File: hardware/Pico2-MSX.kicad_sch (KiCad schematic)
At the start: 63 parts, among them J1 DEBUG, J2 USB_C, SW1 BOOT, U1 MCP4922-ESL, U2 TXB0108PW, U3 W25Q128JVS, U4 W25Q128JVS, U6 RP2350_80QFN, U7 MC74LCX32DTR2G, U8 AMS1117-3.3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

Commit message: Improving the 1v1 circuit
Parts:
- C16, C17: footprint Capacitor_SMD:C_0603_1608Metric -> Additional:C_0603_1608Metric_small
- L1: footprint Inductor_SMD:L_1008_2520Metric -> Additional:L_pol_2016
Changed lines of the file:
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@@
 			)
 		)
-		(property "Footprint" "Inductor_SMD:L_1008_2520Metric"
+		(property "Footprint" "Additional:L_pol_2016"
 			(at 144.78 107.95 0)
 			(effects
@@
 			)
 		)
-		(property "Footprint" "Capacitor_SMD:C_0603_1608Metric"
+		(property "Footprint" "Additional:C_0603_1608Metric_small"
 			(at 133.0452 111.76 0)
 			(effects
@@
 			)
 		)
-		(property "Footprint" "Capacitor_SMD:C_0603_1608Metric"
+		(property "Footprint" "Additional:C_0603_1608Metric_small"
 			(at 120.3452 111.76 0)
 			(effects

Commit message: Delete via for flash memory
And other small modifications (reference at JLCPCB)
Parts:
- J1: LCSC (none) -> C24980
- J2: LCSC C5362630 -> C2988369
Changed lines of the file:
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@@
 			)
 		)
-		(property "LCSC" "C5362630"
+		(property "LCSC" "C2988369"
 			(at 40.64 50.8 0)
 			(effects
@@
 			(at 138.43 179.07 0)
 			(effects
+				(font
+					(size 1.27 1.27)
+				)
+				(hide yes)
+			)
+		)
+		(property "LCSC" "C24980"
+			(at 138.43 179.07 0)
+			(effects

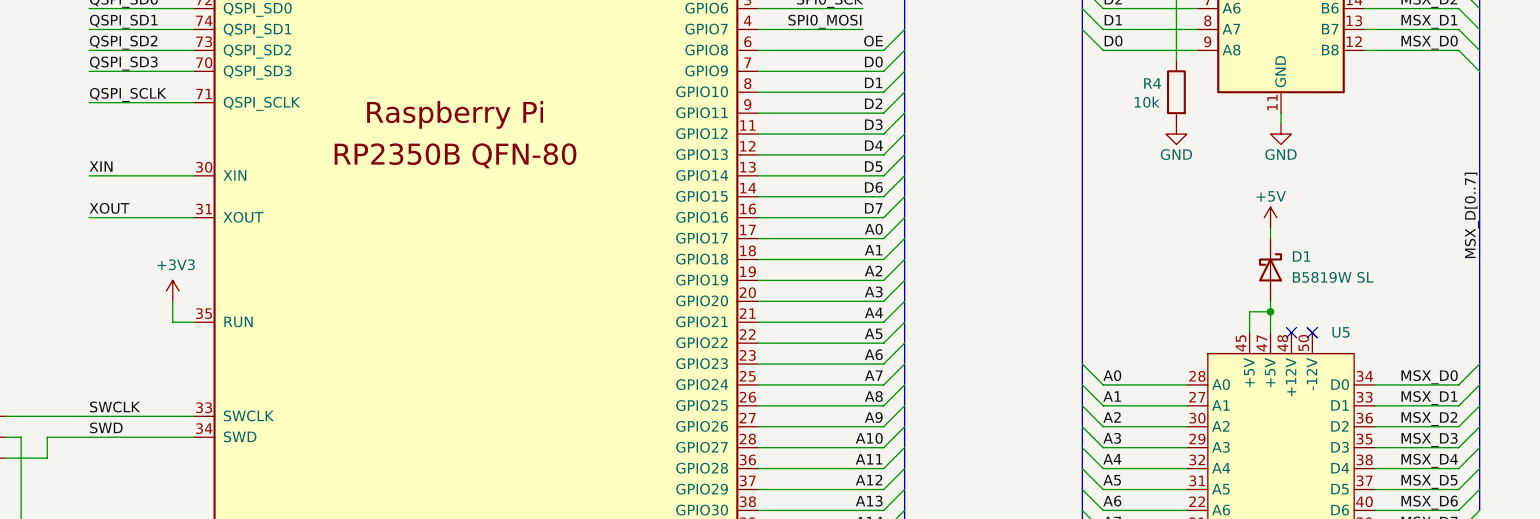
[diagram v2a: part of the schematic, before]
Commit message: Cost reduction and correction of fixing hole placement
- The via are now at a minimum hole size of 0.25.
- The 0201 capacitors have been replaced by 0402s.
- The fixing holes have been moved to a position closer to the standard.
- The tracks have been widened outside the RP2350 area.
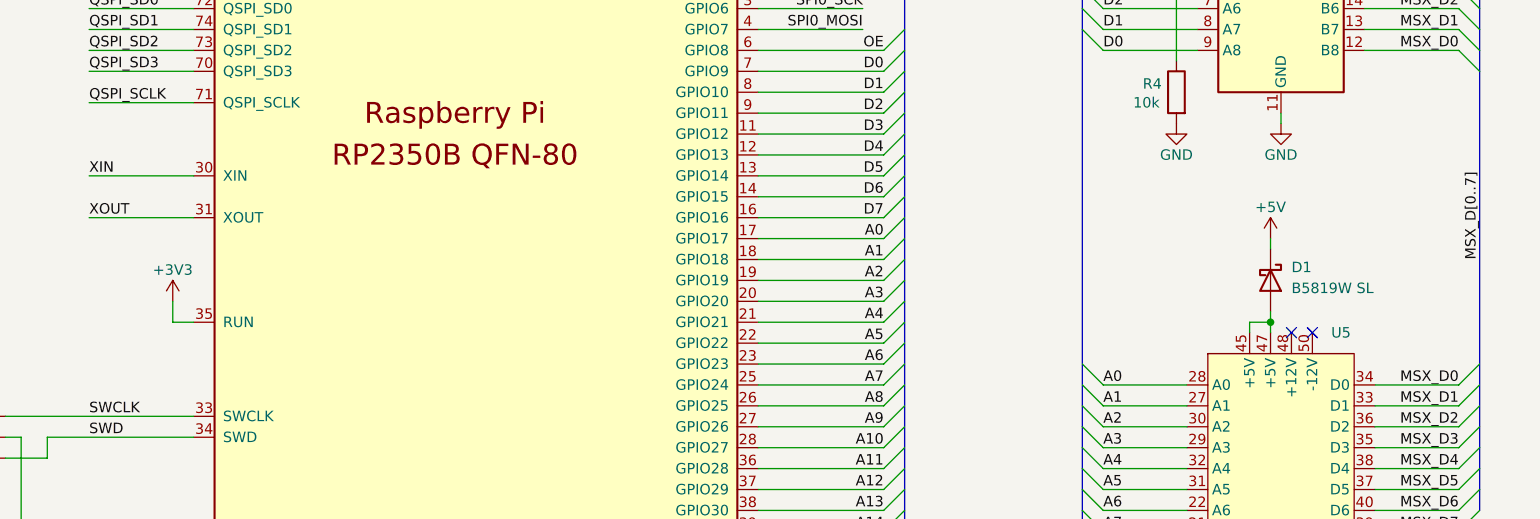
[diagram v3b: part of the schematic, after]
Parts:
- C10, C11, C12, C13, C14, C19, C20, C21, C22, C5, C6, C7: footprint Capacitor_SMD:C_0201_0603Metric -> Additional:C_0402_1005Metric_thin; LCSC C307380 -> C307331
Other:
- moved on the sheet: D1
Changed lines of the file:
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@@
 	)
 	(junction
+		(at 297.18 165.1)
+		(diameter 0)
+		(color 0 0 0 0)
+	)
+	(junction
 		(at 279.4 71.12)
 		(diameter 0)
@@
 	)
 	(junction
-		(at 297.18 163.83)
-		(diameter 0)
-		(color 0 0 0 0)
-	)
-	(junction
 		(at 144.78 35.56)
 		(diameter 0)
@@
 	(wire
 		(pts
+			(xy 297.18 165.1) (xy 297.18 166.37)
+		)
+		(stroke
+			(width 0)
+			(type default)
+		)
+	)
+	(wire
+		(pts
 			(xy 199.39 81.28) (xy 201.93 81.28)
 		)
@@
 	(wire
 		(pts
-			(xy 294.64 163.83) (xy 297.18 163.83)
+			(xy 294.64 165.1) (xy 297.18 165.1)
 		)
 		(stroke
@@
 	(wire
 		(pts
-			(xy 294.64 166.37) (xy 294.64 163.83)
+			(xy 294.64 166.37) (xy 294.64 165.1)
 		)
 		(stroke
@@
 	(wire
 		(pts
-			(xy 297.18 162.56) (xy 297.18 163.83)
-		)
-		(stroke
-			(width 0)
-			(type default)
-		)
-	)
-	(wire
-		(pts
 			(xy 80.01 130.81) (xy 92.71 130.81)
 		)
@@
 	(wire
 		(pts
-			(xy 297.18 153.67) (xy 297.18 154.94)
+			(xy 297.18 154.94) (xy 297.18 156.21)
 		)
 		(stroke
@@
 	(wire
 		(pts
-			(xy 297.18 163.83) (xy 297.18 166.37)
+			(xy 297.18 163.83) (xy 297.18 165.1)
 		)
 		(stroke
@@
 			)
 		)
-		(property "Footprint" "Capacitor_SMD:C_0201_0603Metric"
+		(property "Footprint" "Additional:C_0402_1005Metric_thin"
 			(at 254.9652 69.85 0)
 			(effects
@@
 			)
 		)
-		(property "LCSC" "C307380"
+		(property "LCSC" "C307331"
 			(at 254 66.04 0)
 			(effects
@@
 			)
 		)
-		(property "Footprint" "Capacitor_SMD:C_0201_0603Metric"
+		(property "Footprint" "Additional:C_0402_1005Metric_thin"
 			(at 267.6652 69.85 0)
 			(effects
@@
 			)
 		)
-		(property "LCSC" "C307380"
+		(property "LCSC" "C307331"
 			(at 266.7 66.04 0)
 			(effects
@@
 			)
 		)
-		(property "Footprint" "Capacitor_SMD:C_0201_0603Metric"
+		(property "Footprint" "Additional:C_0402_1005Metric_thin"
 			(at 280.3652 69.85 0)
 			(effects
@@
 			)
 		)
-		(property "LCSC" "C307380"
+		(property "LCSC" "C307331"
 			(at 279.4 66.04 0)
 			(effects
@@
 			)
 		)
-		(property "Footprint" "Capacitor_SMD:C_0201_0603Metric"
+		(property "Footprint" "Additional:C_0402_1005Metric_thin"
 			(at 293.0652 69.85 0)
 			(effects
@@
 			)
 		)
-		(property "LCSC" "C307380"
+		(property "LCSC" "C307331"
 			(at 292.1 66.04 0)
 			(effects
@@
 			)
 		)
-		(property "Footprint" "Capacitor_SMD:C_0201_0603Metric"
+		(property "Footprint" "Additional:C_0402_1005Metric_thin"
 			(at 305.7652 69.85 0)
 			(effects
@@
 			)
 		)
-		(property "LCSC" "C307380"
+		(property "LCSC" "C307331"
 			(at 304.8 66.04 0)
 			(effects
@@
 			)
 		)
-		(property "Footprint" "Capacitor_SMD:C_0201_0603Metric"
+		(property "Footprint" "Additional:C_0402_1005Metric_thin"
 			(at 318.4652 69.85 0)
 			(effects
@@
 			)
 		)
-		(property "LCSC" "C307380"
+		(property "LCSC" "C307331"
 			(at 317.5 66.04 0)
 			(effects
@@
 			)
 		)
-		(property "Footprint" "Capacitor_SMD:C_0201_0603Metric"
+		(property "Footprint" "Additional:C_0402_1005Metric_thin"
 			(at 164.7952 69.85 0)
 			(effects
@@
 			)
 		)
-		(property "LCSC" "C307380"
+		(property "LCSC" "C307331"
 			(at 163.83 66.04 0)
 			(effects
@@
 			)
 		)
-		(property "Footprint" "Capacitor_SMD:C_0201_0603Metric"
+		(property "Footprint" "Additional:C_0402_1005Metric_thin"
 			(at 242.2652 69.85 0)
 			(effects
@@
 			)
 		)
-		(property "LCSC" "C307380"
+		(property "LCSC" "C307331"
 			(at 241.3 66.04 0)
 			(effects
@@
 			)
 		)
-		(property "Footprint" "Capacitor_SMD:C_0201_0603Metric"
+		(property "Footprint" "Additional:C_0402_1005Metric_thin"
 			(at 331.1652 69.85 0)
 			(effects
@@
 			)
 		)
-		(property "LCSC" "C307380"
+		(property "LCSC" "C307331"
 			(at 330.2 66.04 0)
 			(effects
@@
 		)
 		(property "Value" "+3V3"
-			(at 164.211 158.1658 0)
+			(at 163.83 158.75 0)
 			(effects
 				(font
@@
 	(symbol
 		(lib_id "power:+5V")
-		(at 297.18 153.67 0)
+		(at 297.18 154.94 0)
 		(unit 1)
 		(exclude_from_sim no)
@@
 		(dnp no)
 		(property "Reference" "#PWR033"
-			(at 297.18 157.48 0)
+			(at 297.18 158.75 0)
 			(effects
 				(font
@@
 		)
 		(property "Value" "+5V"
-			(at 297.18 149.86 0)
+			(at 297.18 151.13 0)
 			(effects
 				(font
@@
 		)
 		(property "Footprint" ""
-			(at 297.18 153.67 0)
+			(at 297.18 154.94 0)
 			(effects
 				(font
@@
 		)
 		(property "Datasheet" ""
-			(at 297.18 153.67 0)
+			(at 297.18 154.94 0)
 			(effects
 				(font
@@
 		)
 		(property "Description" "Power symbol creates a global label with name \"+5V\""
-			(at 297.18 153.67 0)
+			(at 297.18 154.94 0)
 			(effects
 				(font
@@
 			)
 		)
-		(property "Footprint" "Capacitor_SMD:C_0201_0603Metric"
+		(property "Footprint" "Additional:C_0402_1005Metric_thin"
 			(at 139.3952 69.85 0)
 			(effects
@@
 			)
 		)
-		(property "LCSC" "C307380"
+		(property "LCSC" "C307331"
 			(at 138.43 66.04 0)
 			(effects
@@
 			)
 		)
-		(property "Footprint" "Capacitor_SMD:C_0201_0603Metric"
+		(property "Footprint" "Additional:C_0402_1005Metric_thin"
 			(at 152.0952 69.85 0)
 			(effects
@@
 			)
 		)
-		(property "LCSC" "C307380"
+		(property "LCSC" "C307331"
 			(at 151.13 66.04 0)
 			(effects
@@
 			)
 		)
-		(property "Footprint" "Capacitor_SMD:C_0201_0603Metric"
+		(property "Footprint" "Additional:C_0402_1005Metric_thin"
 			(at 229.5652 69.85 0)
 			(effects
@@
 			)
 		)
-		(property "LCSC" "C307380"
+		(property "LCSC" "C307331"
 			(at 228.6 66.04 0)
 			(effects
@@
 	(symbol
 		(lib_id "Device:D_Schottky")
-		(at 297.18 158.75 270)
+		(at 297.18 160.02 270)
 		(unit 1)
 		(exclude_from_sim no)
@@
 		(fields_autoplaced yes)
 		(property "Reference" "D1"
-			(at 299.72 157.1624 90)
+			(at 299.72 158.4324 90)
 			(effects
 				(font
@@
 		)
 		(property "Value" "B5819W SL"
-			(at 299.72 159.7024 90)
+			(at 299.72 160.9724 90)
 			(effects
 				(font
@@
 		)
 		(property "Footprint" "Diode_SMD:D_SOD-123"
-			(at 297.18 158.75 0)
+			(at 297.18 160.02 0)
 			(effects
 				(font
@@
 		)
 		(property "Datasheet" "~"
-			(at 297.18 158.75 0)
+			(at 297.18 160.02 0)
 			(effects
 				(font
@@
 		)
 		(property "Description" "Schottky diode"
-			(at 297.18 158.75 0)
+			(at 297.18 160.02 0)
 			(effects
 				(font
@@
 		)
 		(property "LCSC" "C8598"
-			(at 297.18 158.75 0)
+			(at 297.18 160.02 0)
 			(effects
 				(font
@@
 		)
 		(property "Manufacturer" "Jiangsu Changjing Electronics Technology Co., Ltd."
-			(at 297.18 158.75 90)
+			(at 297.18 160.02 90)
 			(effects
 				(font
